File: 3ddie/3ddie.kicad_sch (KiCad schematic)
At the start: 58 parts, among them J1 USB4105-GF-A, J2 TRS_MIDI_IN, J3 TRS_MIDI_OUT, J4 Conn_02x11_Counter_Clockwise, U1 W25Q128JV, U2 RP2040, U3 MCP1702T-3302E_CB, U4 MGC3130-I/MQ, U5 MCP1416R, U6 6N137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

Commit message: continued routing
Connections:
- net D+: now reaches J1.A6 (D+), J1.B6 (D+), R6.1
- net D-: now reaches J1.A7 (D-), J1.B7 (D-), R5.1
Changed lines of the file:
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@@
+    (effects (font (size 1.27 1.27)) (justify left bottom))
+  )
+  (label "D-" (at 50.165 36.83 0)
     (effects (font (size 1.27 1.27)) (justify left bottom))
   )
@@
     (effects (font (size 1.27 1.27)) (justify left bottom))
   )
+  (label "D+" (at 50.165 41.91 0)
+    (effects (font (size 1.27 1.27)) (justify left bottom))
+  )

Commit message: layout and schema changes
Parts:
- removed J4: Conn_02x11_Counter_Clockwise, Connector_PinSocket_2.54mm:PinSocket_2x11_P2.54mm_Horizontal, symbol Connector_Generic:Conn_02x11_Counter_Clockwise
- added J4: Conn_02x15_Odd_Even, Connector_IDC:IDC-Header_2x15_P2.54mm_Horizontal, symbol Connector_Generic:Conn_02x15_Odd_Even
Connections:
- net GPIO28 is gone; now on net POT1: U2.40 (GPIO28/ADC2)
- net GPIO29 is gone; now on net POT2: U2.41 (GPIO29/ADC3)
- net +3V3: now also J4.2 (Pin_2), J4.4 (Pin_4)
- net BOOT: now also J4.5 (Pin_5)
- net GND: now also J4.1 (Pin_1), J4.3 (Pin_3)
- net GPIO10: now also J4.22 (Pin_22)
- net GPIO11: now also J4.21 (Pin_21)
- net GPIO15: now also J4.20 (Pin_20)
- net GPIO16: now also J4.19 (Pin_19)
- net GPIO17: now also J4.18 (Pin_18)
- net GPIO18: now also J4.17 (Pin_17)
- net GPIO19: now also J4.16 (Pin_16)
- net GPIO2: now also J4.30 (Pin_30)
- net GPIO20: now also J4.15 (Pin_15)
- net GPIO21: now also J4.14 (Pin_14)
- net GPIO22: now also J4.13 (Pin_13)
- net GPIO23: now also J4.12 (Pin_12)
- net GPIO24: now also J4.11 (Pin_11)
- net GPIO3: now also J4.29 (Pin_29)
- net GPIO4: now also J4.28 (Pin_28)
- net GPIO5: now also J4.27 (Pin_27)
- net GPIO6: now also J4.26 (Pin_26)
- net GPIO7: now also J4.25 (Pin_25)
- net GPIO8: now also J4.24 (Pin_24)
- net GPIO9: now also J4.23 (Pin_23)
- net POT1: no longer U2.38 (GPIO26/ADC0)
- net POT2: no longer U2.39 (GPIO27/ADC1)
- net RUN: now also J4.7 (Pin_7)
- net VBUS: now also J4.6 (Pin_6), J4.8 (Pin_8)
- new net GPIO26: J4.10 (Pin_10), U2.38 (GPIO26/ADC0)
- new net GPIO27: J4.9 (Pin_9), U2.39 (GPIO27/ADC1)

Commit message: mostly finish routing and layout!
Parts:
- S1, S2: footprint Eclectronics:KXT321LHS -> Eclectronics:TL3301AFxxxxJ
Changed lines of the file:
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@@
     (property "Reference" "S1" (id 0) (at 44.45 77.47 90))
     (property "Value" "RST" (id 1) (at 44.45 80.01 90))
-    (property "Footprint" "Eclectronics:KXT321LHS" (id 2) (at 46.99 76.2 90)
+    (property "Footprint" "Eclectronics:TL3301AFxxxxJ" (id 2) (at 46.99 76.2 90)
       (effects (font (size 1.524 1.524)) hide)
     )
@@
     (property "Reference" "S2" (id 0) (at 44.45 88.9 90))
     (property "Value" "BOOT" (id 1) (at 44.45 91.44 90))
-    (property "Footprint" "Eclectronics:KXT321LHS" (id 2) (at 46.99 87.63 90)
+    (property "Footprint" "Eclectronics:TL3301AFxxxxJ" (id 2) (at 46.99 87.63 90)
       (effects (font (size 1.524 1.524)) hide)
     )
@@
     )
     (path "/5d2df827-ba58-42d3-ae75-4504981e88c0"
-      (reference "S1") (unit 1) (value "RST") (footprint "Eclectronics:KXT321LHS")
+      (reference "S1") (unit 1) (value "RST") (footprint "Eclectronics:TL3301AFxxxxJ")
     )
     (path "/6f28eabb-7de3-44e1-afce-60f4a35d1dea"
-      (reference "S2") (unit 1) (value "BOOT") (footprint "Eclectronics:KXT321LHS")
+      (reference "S2") (unit 1) (value "BOOT") (footprint "Eclectronics:TL3301AFxxxxJ")
     )
     (path "/ee96ba52-31ec-4315-9e3c-7bf0139abbc1"

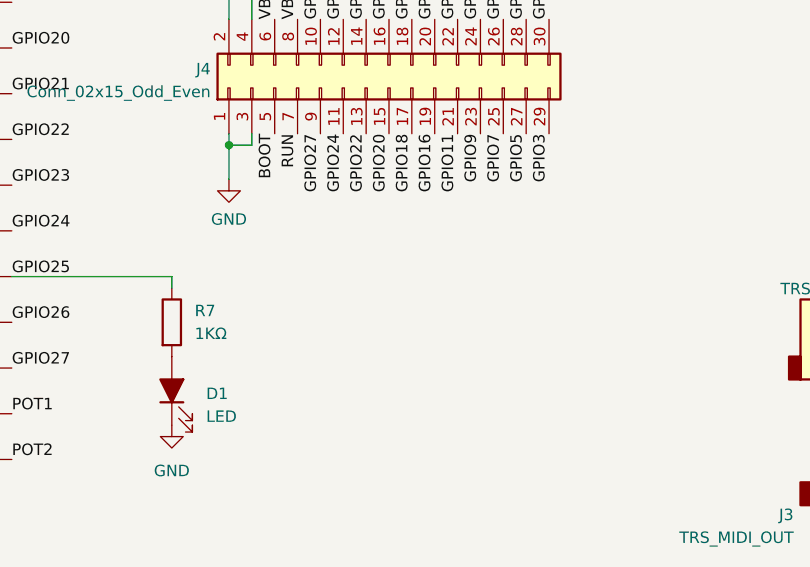
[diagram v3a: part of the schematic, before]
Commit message: clean up routing, add debug header, add silkscreen
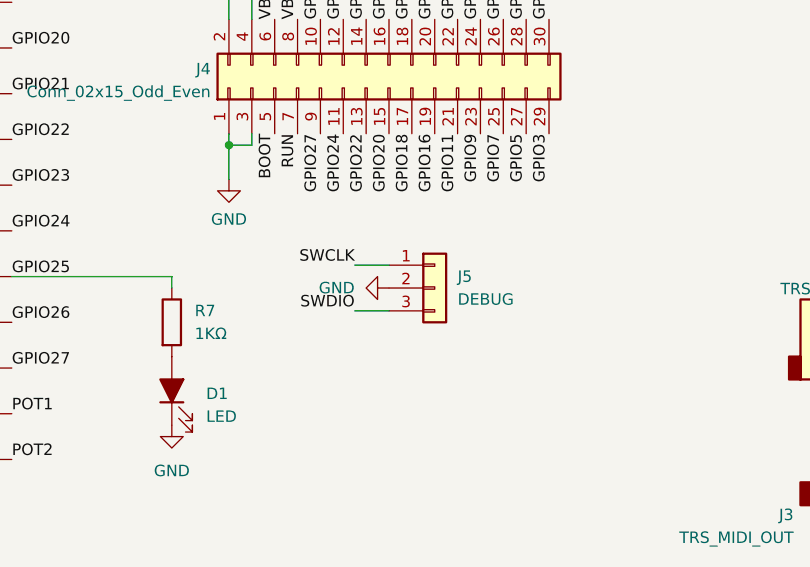
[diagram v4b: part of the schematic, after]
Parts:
- added J5: DEBUG, Connector_PinHeader_2.54mm:PinHeader_1x03_P2.54mm_Vertical, symbol Connector_Generic:Conn_01x03
- RV1, RV2: Digikey Catalog # (none) -> PDB12-H4251-103BF-ND; Manufacturer Part # (none) -> PDB12-H4251-103BF
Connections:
- net GND: now also J5.2 (Pin_2)
- net SWCLK: now also J5.1 (Pin_1)
- net SWDIO: now also J5.3 (Pin_3)
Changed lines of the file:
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@@
+    (stroke (width 0) (type default) (color 0 0 0 0))
+  )
+  (wire (pts (xy 186.69 180.34) (xy 190.5 180.34))
     (stroke (width 0) (type default) (color 0 0 0 0))
   )
@@
     (stroke (width 0) (type default) (color 0 0 0 0))
   )
+  (wire (pts (xy 186.69 175.26) (xy 190.5 175.26))
+    (stroke (width 0) (type default) (color 0 0 0 0))
+  )
   (wire (pts (xy 299.085 177.8) (xy 299.085 180.34))
     (stroke (width 0) (type default) (color 0 0 0 0))
@@
   (wire (pts (xy 67.31 105.41) (xy 87.63 105.41))
     (stroke (width 0) (type default) (color 0 0 0 0))
+  )
+  (label "SWDIO" (at 186.69 180.34 180)
+    (effects (font (size 1.27 1.27)) (justify right bottom))
   )
   (label "GPIO10" (at 198.12 147.955 90)
@@
   (label "GPIO17" (at 193.04 147.955 90)
     (effects (font (size 1.27 1.27)) (justify left bottom))
+  )
+  (label "SWCLK" (at 186.69 175.26 180)
+    (effects (font (size 1.27 1.27)) (justify right bottom))
   )
   (label "GPIO24" (at 148.59 171.45 0)
@@
       (effects (font (size 1.27 1.27)) hide)
     )
-    (property "Datasheet" "~" (id 3) (at 282.575 32.385 0)
+    (property "Datasheet" "https://www.bourns.com/docs/Product-Datasheets/PDB12.pdf" (id 3) (at 282.575 32.385 0)
+      (effects (font (size 1.27 1.27)) hide)
+    )
+    (property "Digikey Catalog #" "PDB12-H4251-103BF-ND" (id 4) (at 282.575 32.385 0)
+      (effects (font (size 1.27 1.27)) hide)
+    )
+    (property "Manufacturer Part #" "PDB12-H4251-103BF" (id 5) (at 282.575 32.385 0)
       (effects (font (size 1.27 1.27)) hide)
     )
@@
     (pin "1")
   )
+  (symbol (lib_id "Connector_Generic:Conn_01x03") (at 195.58 177.8 0) (unit 1)
+    (in_bom yes) (on_board yes) (fields_autoplaced)
+    (property "Reference" "J5" (id 0) (at 198.12 176.5299 0)
+      (effects (font (size 1.27 1.27)) (justify left))
+    )
+    (property "Value" "DEBUG" (id 1) (at 198.12 179.0699 0)
+      (effects (font (size 1.27 1.27)) (justify left))
+    )
+    (property "Footprint" "Connector_PinHeader_2.54mm:PinHeader_1x03_P2.54mm_Vertical" (id 2) (at 195.58 177.8 0)
+      (effects (font (size 1.27 1.27)) hide)
+    )
+    (property "Datasheet" "https://app.adam-tech.com/products/download/data_sheet/203217/bhr-xx-hua-data-sheet.pdf" (id 3) (at 195.58 177.8 0)
+      (effects (font (size 1.27 1.27)) hide)
+    )
+    (property "Digikey Catalog #" "2057-BHR-30-HUA-ND" (id 4) (at 195.58 177.8 0)
+      (effects (font (size 1.27 1.27)) hide)
+    )
+    (property "Manufacturer Part #" "BHR-30-HUA" (id 5) (at 195.58 177.8 0)
+      (effects (font (size 1.27 1.27)) hide)
+    )
+    (pin "1")
+    (pin "2")
+    (pin "3")
+  )
   (symbol (lib_id "3ddie:MGC3130-I{brace}slash}MQ") (at 226.06 77.47 0) (unit 1)
     (in_bom yes) (on_board yes) (fields_autoplaced)
@@
     (pin "2")
   )
+  (symbol (lib_id "power:GND") (at 190.5 177.8 270) (unit 1)
+    (in_bom yes) (on_board yes) (fields_autoplaced)
+    (property "Reference" "#PWR039" (id 0) (at 184.15 177.8 0)
+      (effects (font (size 1.27 1.27)) hide)
+    )
+    (property "Value" "GND" (id 1) (at 186.69 177.7999 90)
+      (effects (font (size 1.27 1.27)) (justify right))
+    )
+    (property "Footprint" "" (id 2) (at 190.5 177.8 0)
+      (effects (font (size 1.27 1.27)) hide)
+    )
+    (property "Datasheet" "" (id 3) (at 190.5 177.8 0)
+      (effects (font (size 1.27 1.27)) hide)
+    )
+    (pin "1")
+  )
   (symbol (lib_id "Device:C") (at 214.63 34.29 0) (unit 1)
     (in_bom yes) (on_board yes) (fields_autoplaced)
@@
       (effects (font (size 1.27 1.27)) hide)
     )
-    (property "Datasheet" "~" (id 3) (at 266.065 32.385 0)
+    (property "Datasheet" "https://www.bourns.com/docs/Product-Datasheets/PDB12.pdf" (id 3) (at 266.065 32.385 0)
+      (effects (font (size 1.27 1.27)) hide)
+    )
+    (property "Digikey Catalog #" "PDB12-H4251-103BF-ND" (id 4) (at 266.065 32.385 0)
+      (effects (font (size 1.27 1.27)) hide)
+    )
+    (property "Manufacturer Part #" "PDB12-H4251-103BF" (id 5) (at 266.065 32.385 0)
       (effects (font (size 1.27 1.27)) hide)
     )
@@
       (reference "#PWR038") (unit 1) (value "GND") (footprint "")
     )
+    (path "/ab7aa3ca-1dc7-4437-822e-65a68c16207b"
+      (reference "#PWR039") (unit 1) (value "GND") (footprint "")
+    )
     (path "/9aff65b0-9c5f-4a98-9527-65570f2d76ea"
       (reference "#PWR0101") (unit 1) (value "+3V3") (footprint "")
@@
       (reference "J4") (unit 1) (value "Conn_02x15_Odd_Even") (footprint "Connector_IDC:IDC-Header_2x15_P2.54mm_Horizontal")
     )
+    (path "/a820514c-f35f-4ba9-953d-5b7e64296f26"
+      (reference "J5") (unit 1) (value "DEBUG") (footprint "Connector_PinHeader_2.54mm:PinHeader_1x03_P2.54mm_Vertical")
+    )
     (path "/7ca43cf0-22a3-4ee0-a8c6-940bc048e7d1"

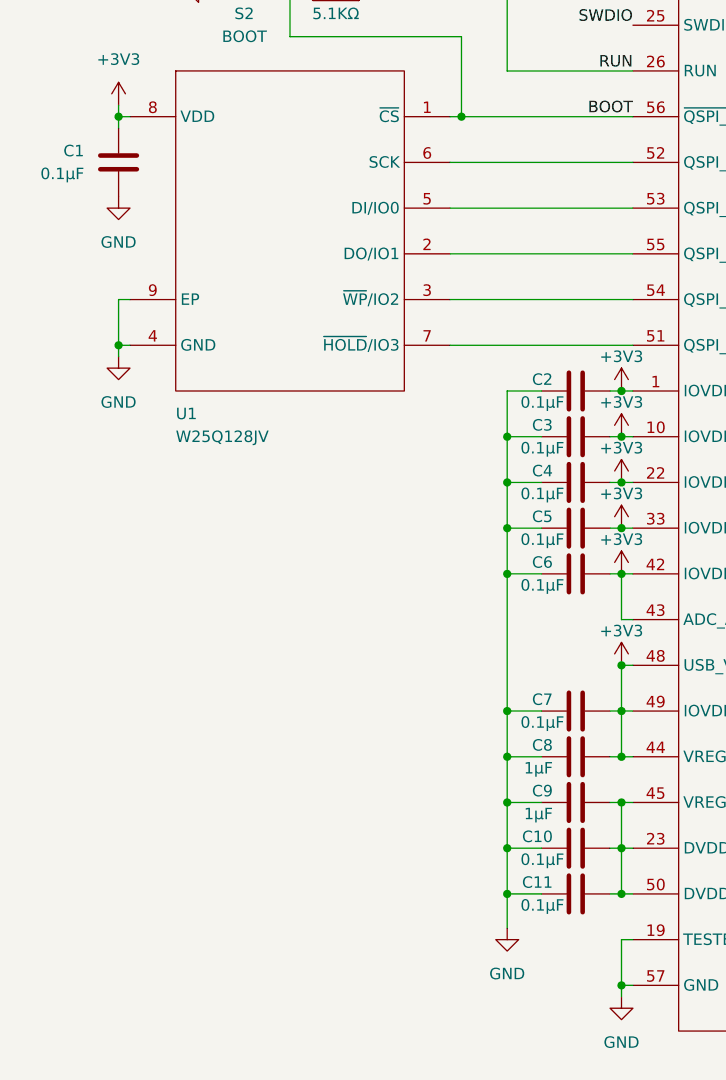
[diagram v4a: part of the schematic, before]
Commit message: fill in missing part numbers for bom prep
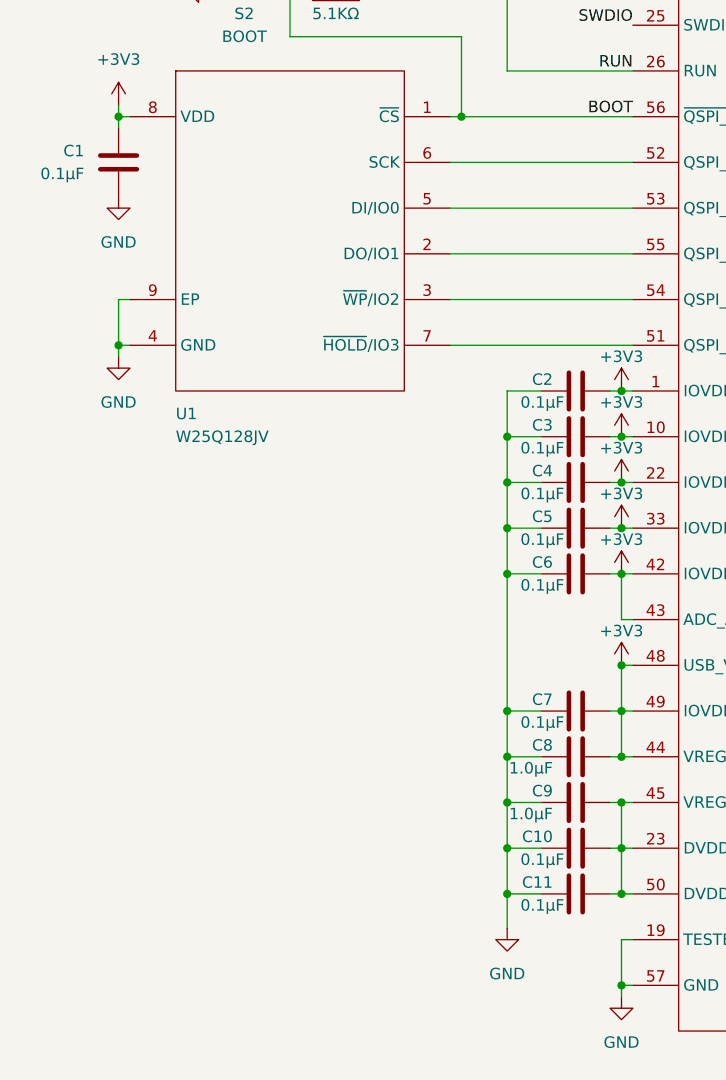
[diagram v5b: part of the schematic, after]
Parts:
- C1: value 0.1µF -> 0.1μF; Digikey Catalog # (none) -> 1276-1033-1-ND; Manufacturer Part # (none) -> CL10B104JB8NNNC
- C10, C11, C2, C3, C4, C5, C6, C7: value 0.1µF -> 0.1μF; Digikey Catalog # (none) -> 1292-1366-1-ND; Manufacturer Part # (none) -> 0402X104K500CT
- C12, C13: Digikey Catalog # (none) -> 490-18214-1-ND; Manufacturer Part # (none) -> GRM188R61E106KA73D
- C14, C18, C20: Digikey Catalog # (none) -> 1276-1033-1-ND; Manufacturer Part # (none) -> CL10B104JB8NNNC
- C15: Digikey Catalog # (none) -> 490-10731-1-ND; Manufacturer Part # (none) -> GRM188R61E225KA12D
- C16, C17: Digikey Catalog # (none) -> 490-7203-1-ND; Manufacturer Part # (none) -> GRM188R61E475KE11D
- C19: Digikey Catalog # (none) -> 1276-1184-1-ND; Manufacturer Part # (none) -> CL10B105KA8NNNC
- C8, C9: value 1µF -> 1.0μF; Digikey Catalog # (none) -> 1276-6796-1-ND; Manufacturer Part # (none) -> CL05A105KL5NRNC
- D1: Manufacturer Part # (none) -> LTST-C170TGKT
- D2: Manufacturer Part # (none) -> LTST-C171KRKT
- J4: Digikey Catalog # (none) -> 2057-BHR-30-HUA-ND; Manufacturer Part # (none) -> BHR-30-HUA
- J5: Digikey Catalog # 2057-BHR-30-HUA-ND -> (none); Manufacturer Part # BHR-30-HUA -> (none)
- R1, R2, R3, R4: Digikey Catalog # (none) -> P5.10KHCT-ND; Manufacturer Part # (none) -> ERJ-3EKF5101V
- R10, R11, R13, R8, R9: Digikey Catalog # (none) -> CR0603-FX-1002ELFCT-ND; Manufacturer Part # (none) -> CR0603-FX-1002ELF
- R12, R7: Digikey Catalog # (none) -> 311-1.00KHRCT-ND; Manufacturer Part # (none) -> RC0603FR-071KL
- R14, R15: Digikey Catalog # (none) -> 311-1.80KHRCT-ND; Manufacturer Part # (none) -> RC0603FR-071K8L
- R16: Digikey Catalog # (none) -> 311-220HRCT-ND; Manufacturer Part # (none) -> RC0603FR-07220RL
- R17: Digikey Catalog # (none) -> 13-RC0603FR-1010RLCT-ND; Manufacturer Part # (none) -> RC0603FR-1010RL
- R18: Digikey Catalog # (none) -> 311-33.0HRCT-ND; Manufacturer Part # (none) -> RC0603FR-0733RL
- R19: Digikey Catalog # (none) -> 311-4.70KHRCT-ND; Manufacturer Part # (none) -> RC0603FR-074K7L
- R5, R6: Digikey Catalog # (none) -> P27.0LCT-ND; Manufacturer Part # (none) -> ERJ-2RKF27R0X

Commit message: exclude debug header from bom
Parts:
- J5: now left out of the parts list
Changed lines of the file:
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@@
   )
   (symbol (lib_id "Connector_Generic:Conn_01x03") (at 195.58 177.8 0) (unit 1)
-    (in_bom yes) (on_board yes) (fields_autoplaced)
+    (in_bom no) (on_board yes) (fields_autoplaced)
     (property "Reference" "J5" (id 0) (at 198.12 176.5299 0)
       (effects (font (size 1.27 1.27)) (justify left))

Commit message: fix incorrect part numbers for buttons
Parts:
- S1, S2: Digikey Catalog # CKN10778CT-ND -> EG4374CT-ND; Manufacturer Part # KTX 321 LHS -> TL3301AF160QJ
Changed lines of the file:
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@@
       (effects (font (size 1.524 1.524)) hide)
     )
-    (property "Digikey Catalog #" "CKN10778CT-ND" (id 4) (at 44.45 74.93 0)
+    (property "Digikey Catalog #" "EG4374CT-ND" (id 4) (at 44.45 74.93 0)
       (effects (font (size 1.27 1.27)) hide)
     )
-    (property "Manufacturer Part #" "KTX 321 LHS" (id 5) (at 44.45 74.93 0)
+    (property "Manufacturer Part #" "TL3301AF160QJ" (id 5) (at 44.45 74.93 0)
       (effects (font (size 1.27 1.27)) hide)
     )
@@
       (effects (font (size 1.524 1.524)) hide)
     )
-    (property "Digikey Catalog #" "CKN10778CT-ND" (id 4) (at 44.45 86.36 0)
+    (property "Digikey Catalog #" "EG4374CT-ND" (id 4) (at 44.45 86.36 0)
       (effects (font (size 1.27 1.27)) hide)
     )
-    (property "Manufacturer Part #" "KTX 321 LHS" (id 5) (at 44.45 86.36 0)
+    (property "Manufacturer Part #" "TL3301AF160QJ" (id 5) (at 44.45 86.36 0)
       (effects (font (size 1.27 1.27)) hide)
     )

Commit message: replace incorrectly sized MGC3130 footprint with correct one, adjust schema and pcb accordingly
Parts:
- U4: footprint 3ddie:MGC3130T-I_MQ -> 3ddie:MGC3130-I_MQ
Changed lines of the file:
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@@
       (effects (font (size 1.524 1.524)) (justify right))
     )
-    (property "Footprint" "3ddie:MGC3130T-I_MQ" (id 2) (at 223.52 124.714 0)
+    (property "Footprint" "3ddie:MGC3130-I_MQ" (id 2) (at 223.52 124.714 0)
       (effects (font (size 1.524 1.524)) hide)
     )
@@
       (effects (font (size 1.524 1.524)))
     )
-    (property "Footprint" "3ddie:MGC3130T-I_MQ" (id 2) (at 251.46 71.374 0)
+    (property "Footprint" "3ddie:MGC3130-I_MQ" (id 2) (at 251.46 71.374 0)
       (effects (font (size 1.524 1.524)) hide)
     )
@@
     )
     (path "/a9329e99-609f-4c39-a02d-48cc774ada87"
-      (reference "U4") (unit 1) (value "MGC3130-I/MQ") (footprint "3ddie:MGC3130T-I_MQ")
+      (reference "U4") (unit 1) (value "MGC3130-I/MQ") (footprint "3ddie:MGC3130-I_MQ")
     )
     (path "/5936d240-6102-4439-994a-788eb8b3c026"
-      (reference "U4") (unit 2) (value "MGC3130-I/MQ") (footprint "3ddie:MGC3130T-I_MQ")
+      (reference "U4") (unit 2) (value "MGC3130-I/MQ") (footprint "3ddie:MGC3130-I_MQ")
     )
     (path "/15b2a124-1eb8-4d1a-932b-488f6e69f5b6"
